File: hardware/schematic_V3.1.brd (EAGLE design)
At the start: 77.7 x 62.1 mm, 22 parts, among them J1 POWER_JACKPTH, J3 ICSP, J4 ICSP, J5 2.54mm, J6 2.54mm, J7 2.54mm, J8 2.54mm, J9 2.54mm, U1 L9110S_DRIVER

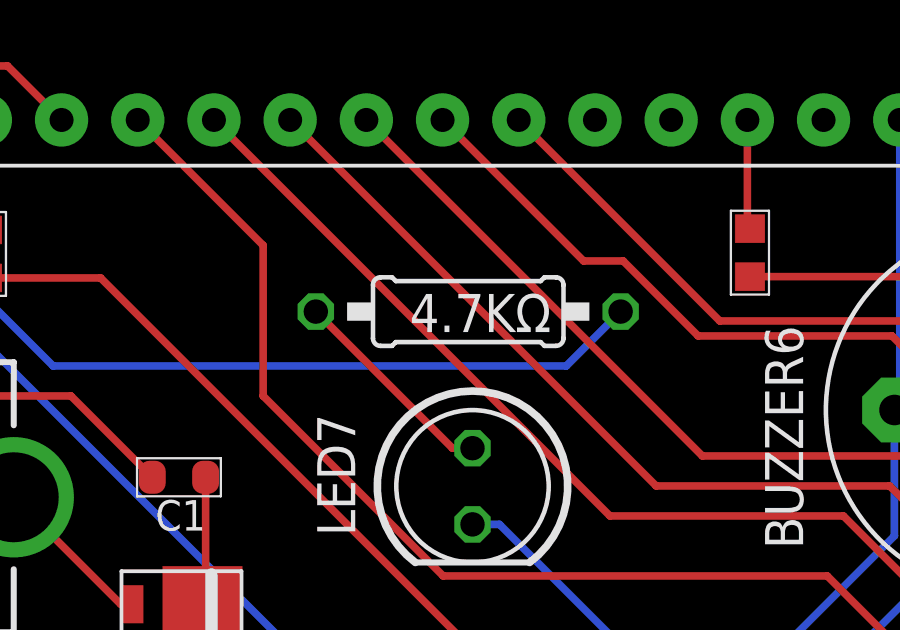
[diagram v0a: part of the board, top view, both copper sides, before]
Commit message: change 4.7K resistor to 470 resistor
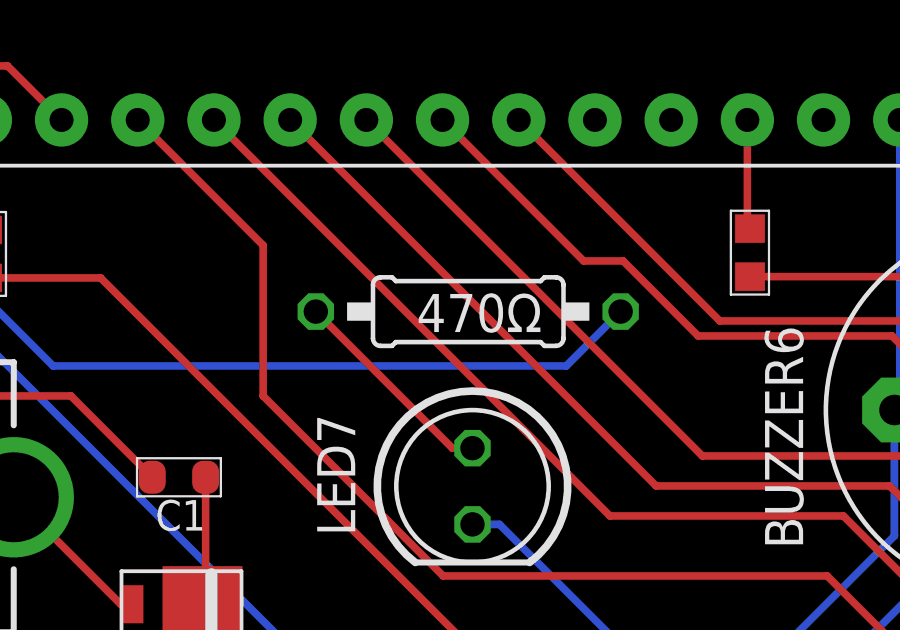
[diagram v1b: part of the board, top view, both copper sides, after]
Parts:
- R1: value 4.7K -> 470
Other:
- board text removed: "4.7KΩ"
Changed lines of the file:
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@@
 <text x="28.8" y="20.4" size="1.27" layer="21" font="vector" ratio="18" rot="R270">LED7</text>
 <text x="60.6" y="18.2" size="1.27" layer="21" font="vector" ratio="18" rot="R90">470Ω</text>
-<text x="36.6" y="24.4" size="1.27" layer="21" font="vector" ratio="18" rot="R180">4.7KΩ</text>
+<text x="36.3" y="24.4" size="1.27" layer="21" font="vector" ratio="18" rot="R180">470Ω</text>
 <rectangle x1="13.382" y1="49.122" x2="13.39" y2="49.126" layer="21"/>
 <rectangle x1="12.822" y1="49.126" x2="12.87" y2="49.13" layer="21"/>
@@
 <attribute name="VALUE" x="58.658" y="41.232" size="1.27" layer="27"/>
 </element>
-<element name="R1" library="barnabas_noggin_V4" package="RESISTOR_PTH" value="4.7K" x="33.836" y="23.812" smashed="yes" rot="R180">
+<element name="R1" library="barnabas_noggin_V4" package="RESISTOR_PTH" value="470" x="33.836" y="23.812" smashed="yes" rot="R180">
 <attribute name="NAME" x="34.784" y="26.088" size="1.016" layer="25" font="vector" rot="R180"/>
 <attribute name="NAME" x="33.836" y="23.812" size="1.27" layer="51" ratio="10" rot="R180" align="center"/>
